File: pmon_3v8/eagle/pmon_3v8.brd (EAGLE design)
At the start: 60 x 60 mm, 39 parts, among them J1 USB, J2 USB, J4 PINHD-1X3, J5 PINHD-2X3, Q1 16Mhz, U1 LTC2943, U2 FT232RL, U3 LT1764AEQ, U4 ATMEGA328TQFP32, U5 TC1015

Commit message: Renamed +4V network to VCC. No semantic change.
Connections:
- net +4V renamed VCC
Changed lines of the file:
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@@
 <wire x1="8.763" y1="36.957" x2="8.8392" y2="36.91" width="0.254" layer="1"/>
 </signal>
-<signal name="+4V">
+<signal name="VCC">
 <contactref element="U5" pad="5"/>
 <contactref element="R1" pad="2"/>

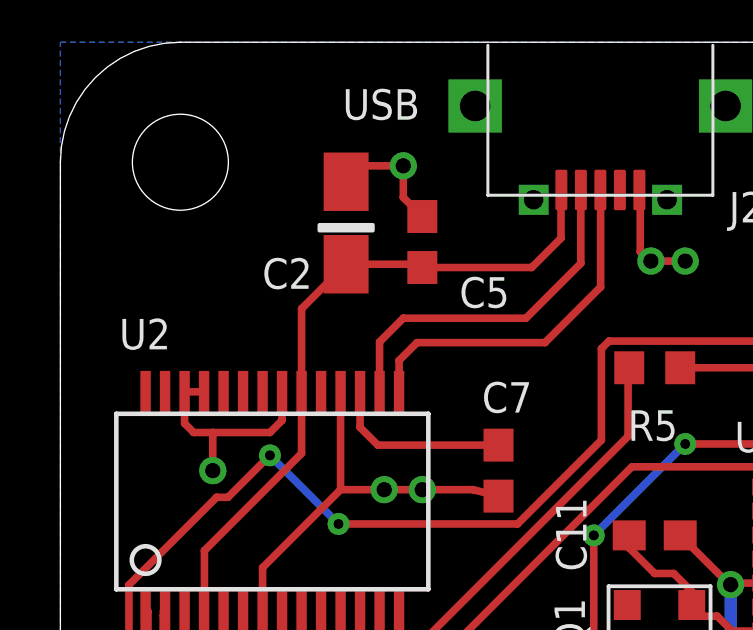
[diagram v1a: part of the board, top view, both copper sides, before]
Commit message: Minor layout change. Reroute a short between two pins to avoid reflow that looks like a solder bridge.
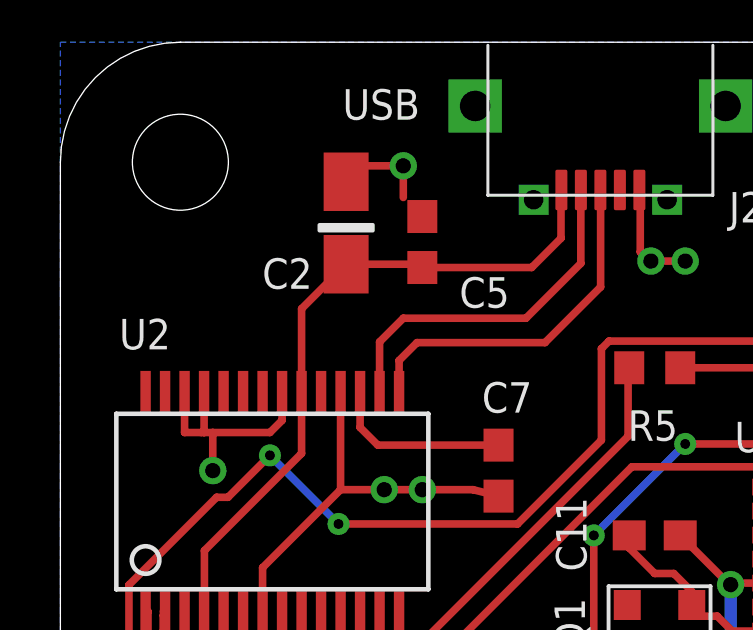
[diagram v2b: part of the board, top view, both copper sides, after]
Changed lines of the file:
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@@
 <wire x1="9.525" y1="55.88" x2="9.525" y2="55.35" width="0.254" layer="1"/>
 <via x="11.43" y="55.88" extent="1-16" drill="0.508"/>
-<wire x1="12.065" y1="54.19" x2="11.43" y2="54.825" width="0.254" layer="1"/>
 <wire x1="11.43" y1="54.825" x2="11.43" y2="55.88" width="0.254" layer="1"/>
 <wire x1="19.3" y1="55.075" x2="19.3294" y2="55.0456" width="0.254" layer="1"/>
@@
 <via x="10.795" y="45.085" extent="1-16" drill="0.508"/>
 <via x="12.065" y="45.085" extent="1-16" drill="0.508"/>
-<wire x1="4.14" y1="48.346" x2="4.14" y2="47.295" width="0.254" layer="1"/>
-<wire x1="4.14" y1="47.295" x2="4.445" y2="46.99" width="0.254" layer="1"/>
-<wire x1="4.445" y1="46.99" x2="5.08" y2="46.99" width="0.254" layer="1"/>
+<wire x1="4.14" y1="48.346" x2="4.14" y2="46.99" width="0.254" layer="1"/>
+<wire x1="4.14" y1="46.99" x2="4.699" y2="46.99" width="0.254" layer="1"/>
+<wire x1="4.79" y1="46.99" x2="5.08" y2="46.99" width="0.254" layer="1"/>
 <wire x1="5.08" y1="46.99" x2="6.985" y2="46.99" width="0.254" layer="1"/>
 <wire x1="6.985" y1="46.99" x2="7.39" y2="47.395" width="0.254" layer="1"/>
 <wire x1="7.39" y1="47.395" x2="7.39" y2="48.346" width="0.254" layer="1"/>
-<wire x1="4.79" y1="48.346" x2="4.14" y2="48.346" width="0.254" layer="1"/>
 <wire x1="5.08" y1="46.99" x2="5.08" y2="45.72" width="0.254" layer="1"/>
 <via x="5.08" y="45.72" extent="1-16" drill="0.508"/>
@@
 <wire x1="36.938053125" y1="50.441559375" x2="36.107" y2="51.2726125" width="0.4064" layer="1"/>
 <wire x1="36.107" y1="51.2726125" x2="36.107" y2="51.816" width="0.4064" layer="1"/>
+<wire x1="4.79" y1="48.346" x2="4.79" y2="46.99" width="0.254" layer="1"/>
+<wire x1="4.79" y1="46.99" x2="4.699" y2="46.99" width="0.254" layer="1"/>
+<wire x1="11.43" y1="54.825" x2="12.065" y2="54.19" width="0" layer="19" extent="1-1"/>
 </signal>
 <signal name="+5V">

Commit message: Add tcream holes for usb connector.
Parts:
- J1, J2: device pmon_oled:USB-MICRO-ZX62RD-AB-5P8 -> pmon_3v8:USB-MICRO-ZX62RD-AB-5P8
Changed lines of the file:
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@@
 <attribute name="NAME" x="40.259" y="33.02" size="1.016" layer="25" font="vector" ratio="10" rot="R180"/>
 </element>
-<element name="J1" library="pmon_oled" package="USB-MICRO-ZX62RD-AB-5P8" value="USB" x="42" y="60.5" smashed="yes" rot="R180">
+<element name="J1" library="pmon_3v8" package="USB-MICRO-ZX62RD-AB-5P8" value="USB" x="42" y="60.5" smashed="yes" rot="R180">
 <attribute name="NAME" x="46.788228125" y="55.17375" size="1.016" layer="25" font="vector" ratio="10"/>
 </element>
@@
 <attribute name="NAME" x="36.926078125" y="25.838915625" size="1.016" layer="25" font="vector" ratio="10"/>
 </element>
-<element name="J2" library="pmon_oled" package="USB-MICRO-ZX62RD-AB-5P8" value="USB" x="18" y="60.5" smashed="yes" rot="R180">
+<element name="J2" library="pmon_3v8" package="USB-MICRO-ZX62RD-AB-5P8" value="USB" x="18" y="60.5" smashed="yes" rot="R180">
 <attribute name="NAME" x="22.285" y="53.99" size="1.016" layer="25" font="vector" ratio="10"/>
 </element>
